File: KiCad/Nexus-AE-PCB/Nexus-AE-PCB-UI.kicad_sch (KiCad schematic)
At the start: 56 parts, among them Q2 2N3904, Q3 2N3904, SW1 SW_Push, SW2 SW_Push, U2 MCP6002T-I_MS, U3 Driver_LED_PCA9633PW,118

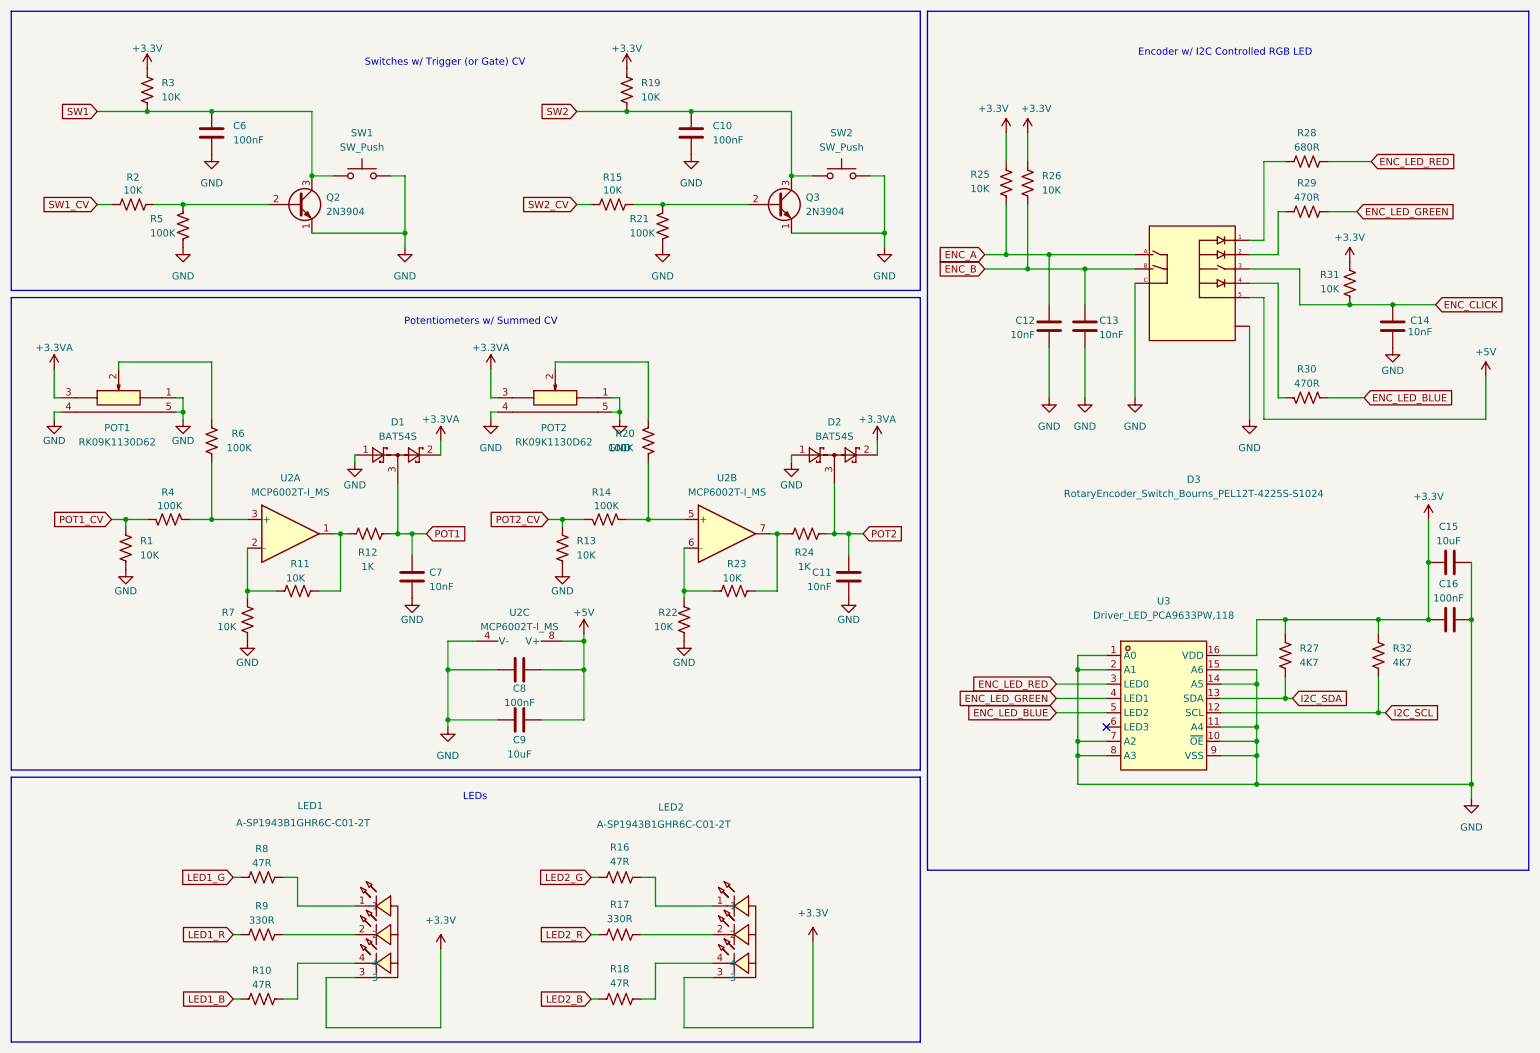
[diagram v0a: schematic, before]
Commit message: PCB and schmeatic are both approx 90% complete
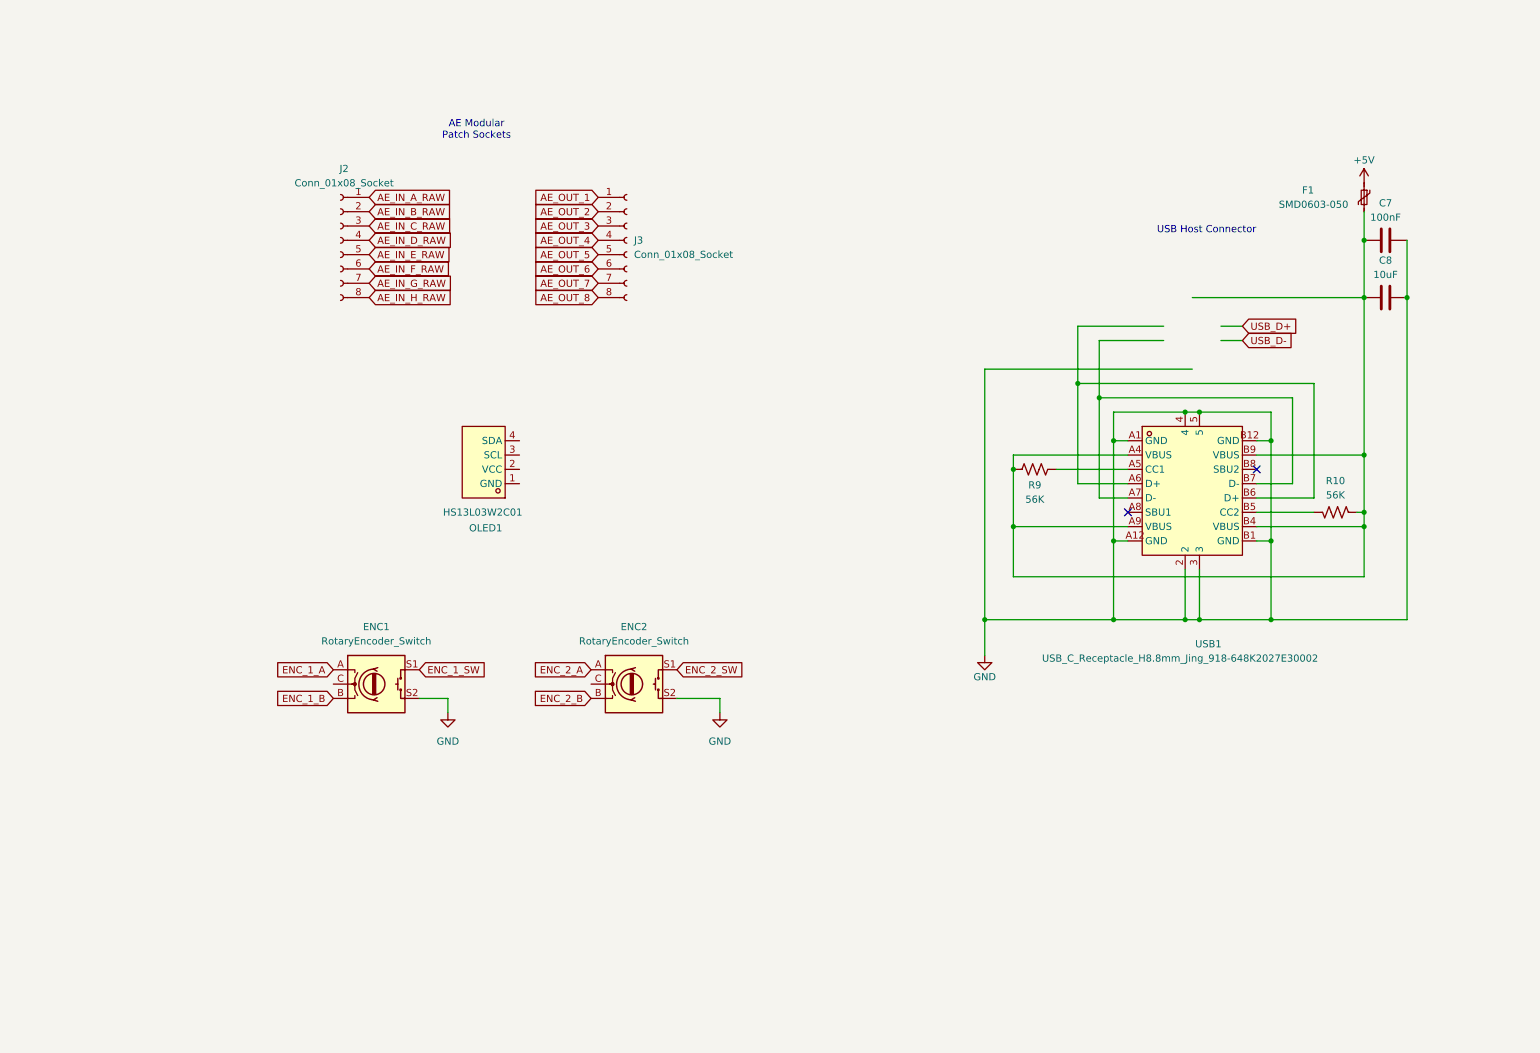
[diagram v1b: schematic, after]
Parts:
- removed C10, C16, C6: 100nF, Capacitor_SMD:C_0603_1608Metric, symbol Device:C
- removed C11, C12, C13, C14: 10nF, Capacitor_SMD:C_0603_1608Metric, symbol Device:C
- removed C15, C9: 10uF, Capacitor_SMD:C_0603_1608Metric, symbol Device:C
- removed D1, D2: BAT54S, Package_TO_SOT_SMD:SOT-23, symbol Diode:BAT54S
- removed D3: RotaryEncoder_Switch_Bourns_PEL12T-4225S-S1024, clectric-diy:RotaryEncoder_Switch_Bourns_PEL12T-4225S-S1024, symbol clectric-diy:RotaryEncoder_Switch_Bourns_PEL12T-4225S-S1024
- removed LED1, LED2: A-SP1943B1GHR6C-C01-2T, clectric-diy:LED_ARGB_Amicc_A-SP1943B1GHR6C-C01-2T, symbol clectric-diy:LED_ARGB_Amicc_A-SP1943B1GHR6C-C01-2T
- removed POT1, POT2: RK09K1130D62, clectric-diy:Potentiometer_THT_Alps_RK09K1130D62, symbol clectric-diy:R_Potentiometer_Alps_RK09K1130D62
- removed Q2, Q3: 2N3904, Package_TO_SOT_THT:TO-92_Inline, symbol Transistor_BJT:2N3904
- removed R1, R11, R13, R15, R19, R2, R22, R23, R25, R26, R3, R31, R7: 10K, Resistor_SMD:R_0603_1608Metric, symbol Device:R_US
- removed R12, R24: 1K, Resistor_SMD:R_0603_1608Metric, symbol Device:R_US
- removed R14, R20, R21, R4, R5, R6: 100K, Resistor_SMD:R_0603_1608Metric, symbol Device:R_US
- removed R16, R18, R8: 47R, Resistor_SMD:R_0603_1608Metric, symbol Device:R_US
- removed R17: 330R, Resistor_SMD:R_0603_1608Metric, symbol Device:R_US
- removed R27, R32: 4K7, Resistor_SMD:R_0603_1608Metric, symbol Device:R_US
- removed R28: 680R, Resistor_SMD:R_0603_1608Metric, symbol Device:R_US
- removed R29, R30: 470R, Resistor_SMD:R_0603_1608Metric, symbol Device:R_US
- removed SW1, SW2: SW_Push, Button_Switch_THT:SW_PUSH_6mm, symbol Switch:SW_Push
- removed U2: MCP6002T-I_MS, clectric-diy:Amplifier_Operational_Microchip_MCP6002T-I_MS, symbol Amplifier_Operational:MCP6002-xMS
- removed U3: Driver_LED_PCA9633PW,118, clectric-diy:TSSOP-16_L5.0-W4.4-P0.64-LS6.4-BL, symbol clectric-diy:Driver_LED_PCA9633PW,118
- added ENC1, ENC2: RotaryEncoder_Switch, Rotary_Encoder:RotaryEncoder_Alps_EC11E-Switch_Vertical_H20mm, symbol Device:RotaryEncoder_Switch
- added F1: SMD0603-050, Fuse:Fuse_0603_1608Metric, symbol Device:Polyfuse_Small
- added J2, J3: Conn_01x08_Socket, Connector_PinSocket_2.54mm:PinSocket_1x08_P2.54mm_Vertical, symbol Connector:Conn_01x08_Socket
- added OLED1: HS13L03W2C01, clectric-diy:OLED-TH_L35.4-W33.5_HS13L03W2C01, symbol clectric-diy:HS13L03W2C01
- added USB1: USB_C_Receptacle_H8.8mm_Jing_918-648K2027E30002, clectric-diy:USB_C_Receptacle_H8.8mm_Jing_918-648K2027E30002, symbol clectric-diy:USB_C_Receptacle_H8.8mm_Jing_918-648K2027E30002
- C7: value 10nF -> 100nF; footprint Capacitor_SMD:C_0603_1608Metric -> Capacitor_SMD:C_0402_1005Metric
- C8: value 100nF -> 10uF; footprint Capacitor_SMD:C_0603_1608Metric -> Capacitor_SMD:C_0402_1005Metric
- R10: value 47R -> 56K; footprint Resistor_SMD:R_0603_1608Metric -> Resistor_SMD:R_0402_1005Metric
- R9: value 330R -> 56K; footprint Resistor_SMD:R_0603_1608Metric -> Resistor_SMD:R_0402_1005Metric
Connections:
- net LED1_R is gone; now on an unnamed net: R9.1
- net POT1 is gone; now on an unnamed net: C7.1
- net +5V: now also F1.1; no longer C8.1
- net GND: now also ENC1.S2, ENC2.S2, USB1.2, USB1.3, USB1.4, USB1.5, USB1.A1 (GND), USB1.A12 (GND), USB1.B1 (GND), USB1.B12 (GND)
- net at R9.2: now also USB1.A5 (CC1)
- net at R10.2: now also USB1.B5 (CC2)
- net LED1_B: no longer names the net of R10.1
- net LED1_B: now also C8.1, F1.2, USB1.A4 (VBUS), USB1.A9 (VBUS), USB1.B4 (VBUS), USB1.B9 (VBUS)
- new net: USB1.A6 (D+), USB1.B6 (D+)
- new net: USB1.A7 (D-), USB1.B7 (D-)
- new net AE_IN_A_RAW: J2.1 (Pin_1)
- new net AE_IN_B_RAW: J2.2 (Pin_2)
- new net AE_IN_C_RAW: J2.3 (Pin_3)
- new net AE_IN_D_RAW: J2.4 (Pin_4)
- new net AE_IN_E_RAW: J2.5 (Pin_5)
- new net AE_IN_F_RAW: J2.6 (Pin_6)
- new net AE_IN_G_RAW: J2.7 (Pin_7)
- new net AE_IN_H_RAW: J2.8 (Pin_8)
- new net AE_OUT_1: J3.1 (Pin_1)
- new net AE_OUT_2: J3.2 (Pin_2)
- new net AE_OUT_3: J3.3 (Pin_3)
- new net AE_OUT_4: J3.4 (Pin_4)
- new net AE_OUT_5: J3.5 (Pin_5)
- new net AE_OUT_6: J3.6 (Pin_6)
- new net AE_OUT_7: J3.7 (Pin_7)
- new net AE_OUT_8: J3.8 (Pin_8)
- new net ENC_1_A: ENC1.A
- new net ENC_1_B: ENC1.B
- new net ENC_1_SW: ENC1.S1
- new net ENC_2_A: ENC2.A
- new net ENC_2_B: ENC2.B
- new net ENC_2_SW: ENC2.S1
- no-connect marks 1 -> 2
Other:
- note added: "AE Modular Patch Sockets"
- note added: "USB Host Connector"
- note removed: "Encoder w/ I2C Controlled RGB LED"
- note removed: "LEDs"
- note removed: "Potentiometers w/ Summed CV"
- note removed: "Switches w/ Trigger (or Gate) CV"
